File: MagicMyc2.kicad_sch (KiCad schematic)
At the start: 27 parts, among them J1 RGB, J2 SPI, J3 PowerSupply, J4 Aout, J5 GPIOs, J6 PRG, J7 MEM2080-00-128-00-A, J8 10102166A812A, Q1 BC338, U1 PIC18F15Q41-I/SS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

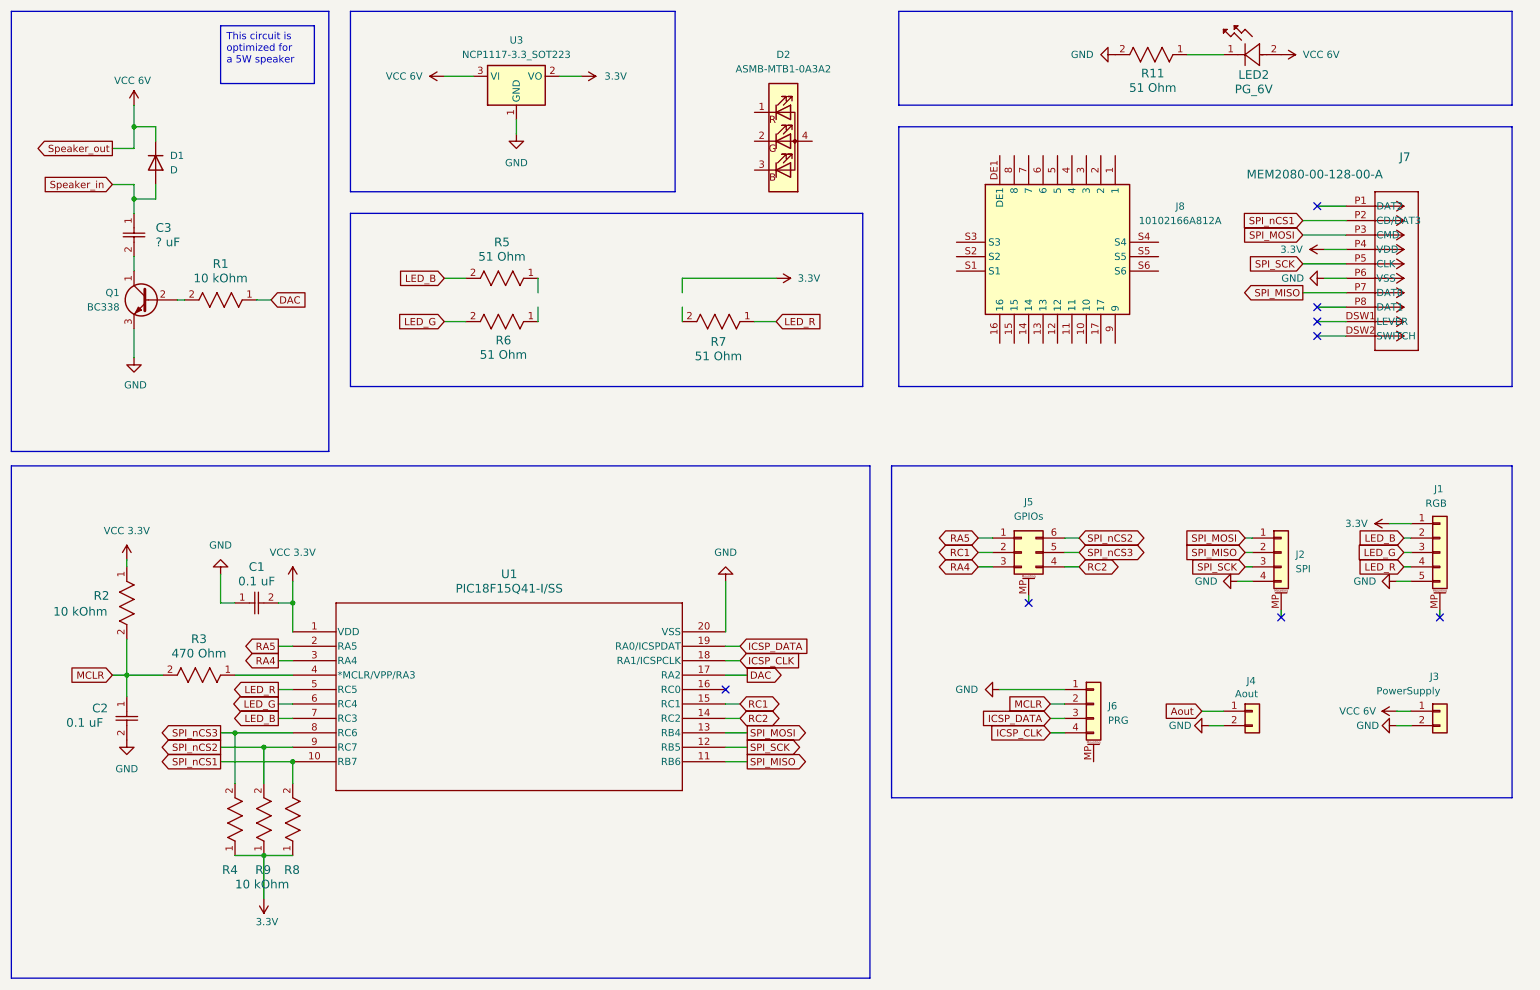
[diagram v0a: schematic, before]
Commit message: v2: changed Pinout, Layout; removed 6V PG-LED
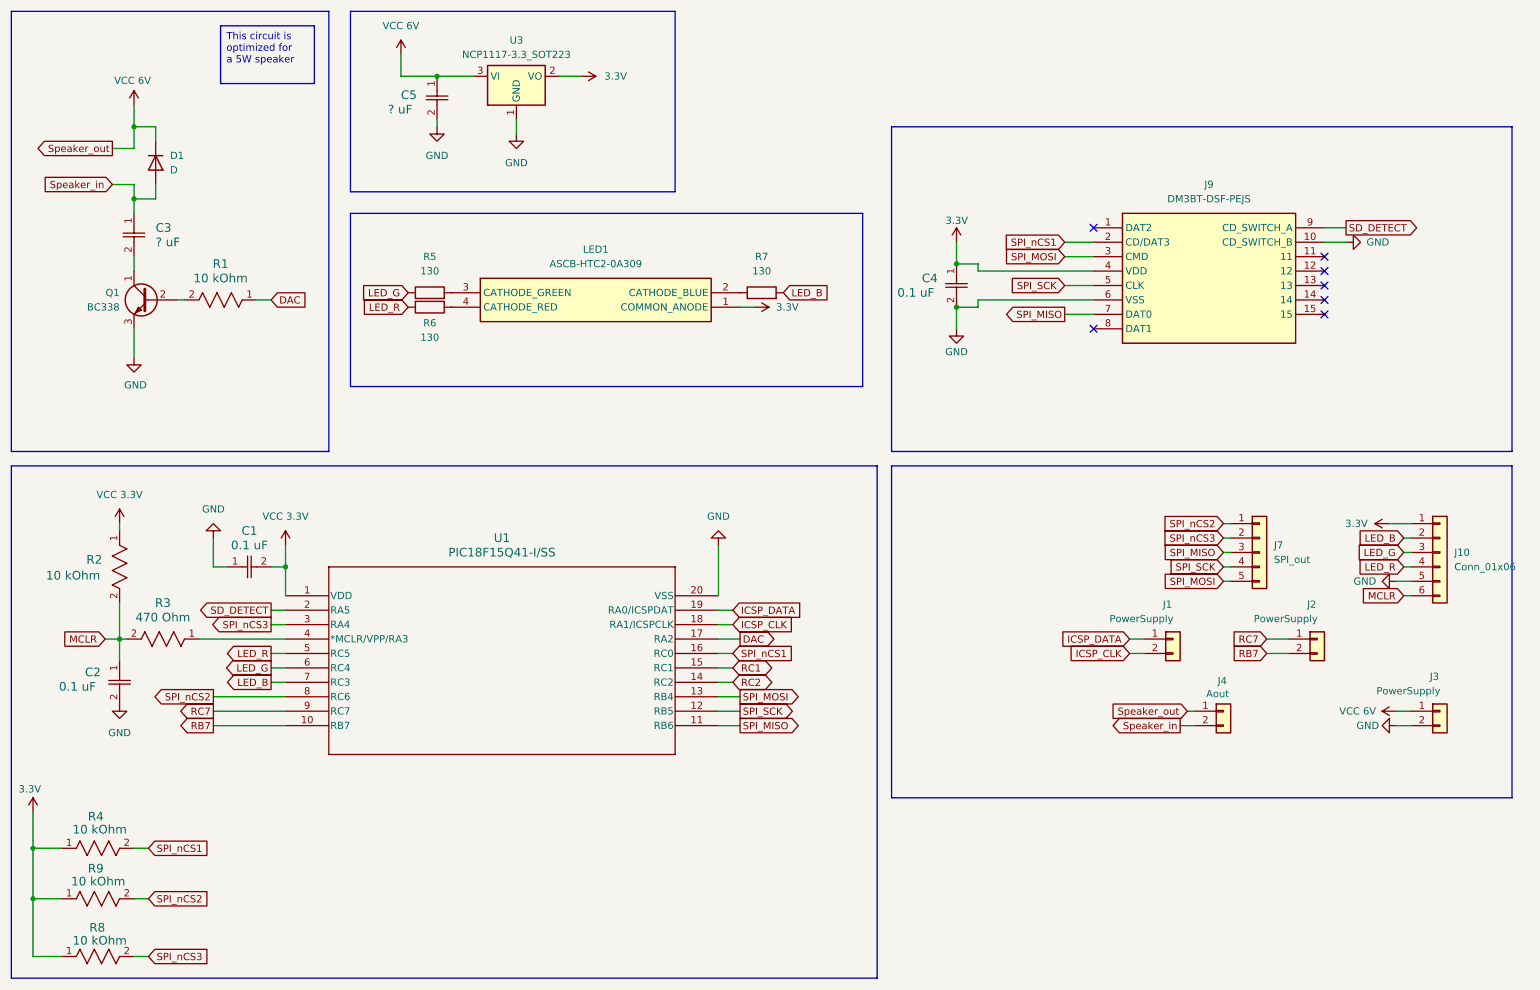
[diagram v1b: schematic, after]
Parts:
- removed D2: ASMB-MTB1-0A3A2, LED_SMD:LED_Wurth_150044M155260, symbol LED:ASMB-MTB1-0A3A2
- removed J1: RGB, Connector_Hirose:Hirose_DF13-05P-1.25DSA_1x05_P1.25mm_Vertical, symbol Connector_Generic_MountingPin:Conn_01x05_MountingPin
- removed J2: SPI, Connector_Hirose:Hirose_DF13-04P-1.25DSA_1x04_P1.25mm_Vertical, symbol Connector_Generic_MountingPin:Conn_01x04_MountingPin
- removed J5: GPIOs, Connector_PinHeader_2.00mm:PinHeader_2x03_P2.00mm_Vertical, symbol Connector_Generic_MountingPin:Conn_02x03_Counter_Clockwise_MountingPin
- removed J6: PRG, Connector_Hirose:Hirose_DF13-04P-1.25DSA_1x04_P1.25mm_Vertical, symbol Connector_Generic_MountingPin:Conn_01x04_MountingPin
- removed J7: MEM2080-00-128-00-A, MEM2080-00-128-00-A:CONN_MEM2080-00-128-00-A_GCT, symbol MEM2080-00-128-00-A:MEM2080-00-128-00-A
- removed J8: 10102166A812A, 10102166A812A, symbol 10102166A812A:10102166A812A
- removed LED2: PG_6V, JB3030AWT-P-B65EA0000-N0000001:LED_J-SERIES_3030_CRW, symbol JB3030AWT-P-B65EA0000-N0000001:JB3030AWT-P-B65EA0000-N0000001
- removed R11, R5, R6, R7: 51 Ohm, RT0603DRE0710KL:RC0603N_YAG, symbol RT0603DRE0751RL:RT0603DRE0751RL
- added C4: 0.1 uF, C0603C103M5RAC7411:CAPC17595_87N_KEM, symbol C0603C103M5RAC7411:C0603C103M5RAC7411
- added C5: ? uF, C0603C103M5RAC7411:CAPC17595_87N_KEM, symbol C0603C103M5RAC7411:C0603C103M5RAC7411
- added J1, J2: PowerSupply, Connector_PinHeader_2.00mm:PinHeader_1x02_P2.00mm_Vertical, symbol Connector_Generic:Conn_01x02
- added J10: Conn_01x06, Connector_PinHeader_2.00mm:PinHeader_1x06_P2.00mm_Vertical, symbol Connector_Generic:Conn_01x06
- added J7: SPI_out, Connector_PinHeader_2.00mm:PinHeader_1x05_P2.00mm_Vertical, symbol Connector_Generic:Conn_01x05
- added J9: DM3BT-DSF-PEJS, Connector_Card:microSD_HC_Hirose_DM3BT-DSF-PEJS, symbol DM3BT-DSF-PEJS:DM3BT-DSF-PEJS
- added LED1: ASCB-HTC2-0A309, ASCB-HTC2-0A309:ASCBHTC20A309, symbol ASCB-HTC2-0A309:ASCB-HTC2-0A309
- added R5, R6, R7: 130, Resistor_SMD:R_0603_1608Metric, symbol Device:R
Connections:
- net Aout is gone; now on net VCC 6V: J4.1 (Pin_1)
- net RA4 is gone; now on net SPI_nCS3: U1.3 (RA4)
- net 3.3V: now also C4.1, J10.1 (Pin_1), J9.4 (VDD), LED1.1 (COMMON_ANODE)
- net GND: now also C4.2, C5.2, J10.5 (Pin_5), J9.10 (CD_SWITCH_B), J9.6 (VSS); no longer J4.2 (Pin_2)
- net ICSP_CLK: now also J1.2 (Pin_2)
- net ICSP_DATA: now also J1.1 (Pin_1)
- net LED_B: now also J10.2 (Pin_2), R7.2
- net LED_G: now also J10.3 (Pin_3), R5.1
- net LED_R: now also J10.4 (Pin_4), R6.2
- net MCLR: now also J10.6 (Pin_6)
- net SPI_MISO: now also J7.3 (Pin_3), J9.7 (DAT0)
- net SPI_MOSI: now also J7.5 (Pin_5), J9.3 (CMD)
- net SPI_SCK: now also J7.4 (Pin_4), J9.5 (CLK)
- net SPI_nCS1: now also R4.2, U1.16 (RC0), J9.2 (CD/DAT3); no longer R8.2, U1.10 (RB7)
- net SPI_nCS2: now also U1.8 (RC6), J7.1 (Pin_1); no longer U1.9 (RC7)
- net SPI_nCS3: now also R8.2, J7.2 (Pin_2); no longer R4.2, U1.8 (RC6)
- net Speaker_in : now also J4.2 (Pin_2)
- net VCC 6V: now also C5.1
- net RA5 renamed SD_DETECT
- net SD_DETECT: now also J9.9 (CD_SWITCH_A)
- new net: LED1.3 (CATHODE_GREEN), R5.2
- new net: LED1.2 (CATHODE_BLUE), R7.1
- new net: LED1.4 (CATHODE_RED), R6.1
- new net RB7: J2.2 (Pin_2), U1.10 (RB7)
- new net RC7: J2.1 (Pin_1), U1.9 (RC7)
- no-connect marks 8 -> 7
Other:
- moved on the sheet: C1, C2, J4, R2, R3, R4, R8, R9, U1

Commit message: added drill holes back
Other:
- moved on the sheet: C4, C5, J9, LED1, R5, R6, R7, U3

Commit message: Updated schematic pdf + some 3D models
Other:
- company: (none) -> Author: Christian R
- title: (none) -> MagicMyc2
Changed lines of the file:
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@@
 	(generator_version "8.0")
 	(paper "A4")
+	(title_block
+		(title "MagicMyc2")
+		(date "26.01.2025")
+		(rev "2")
+		(company "Author: Christian R")
+	)
 	(junction
 		(at 39.37 49.53)

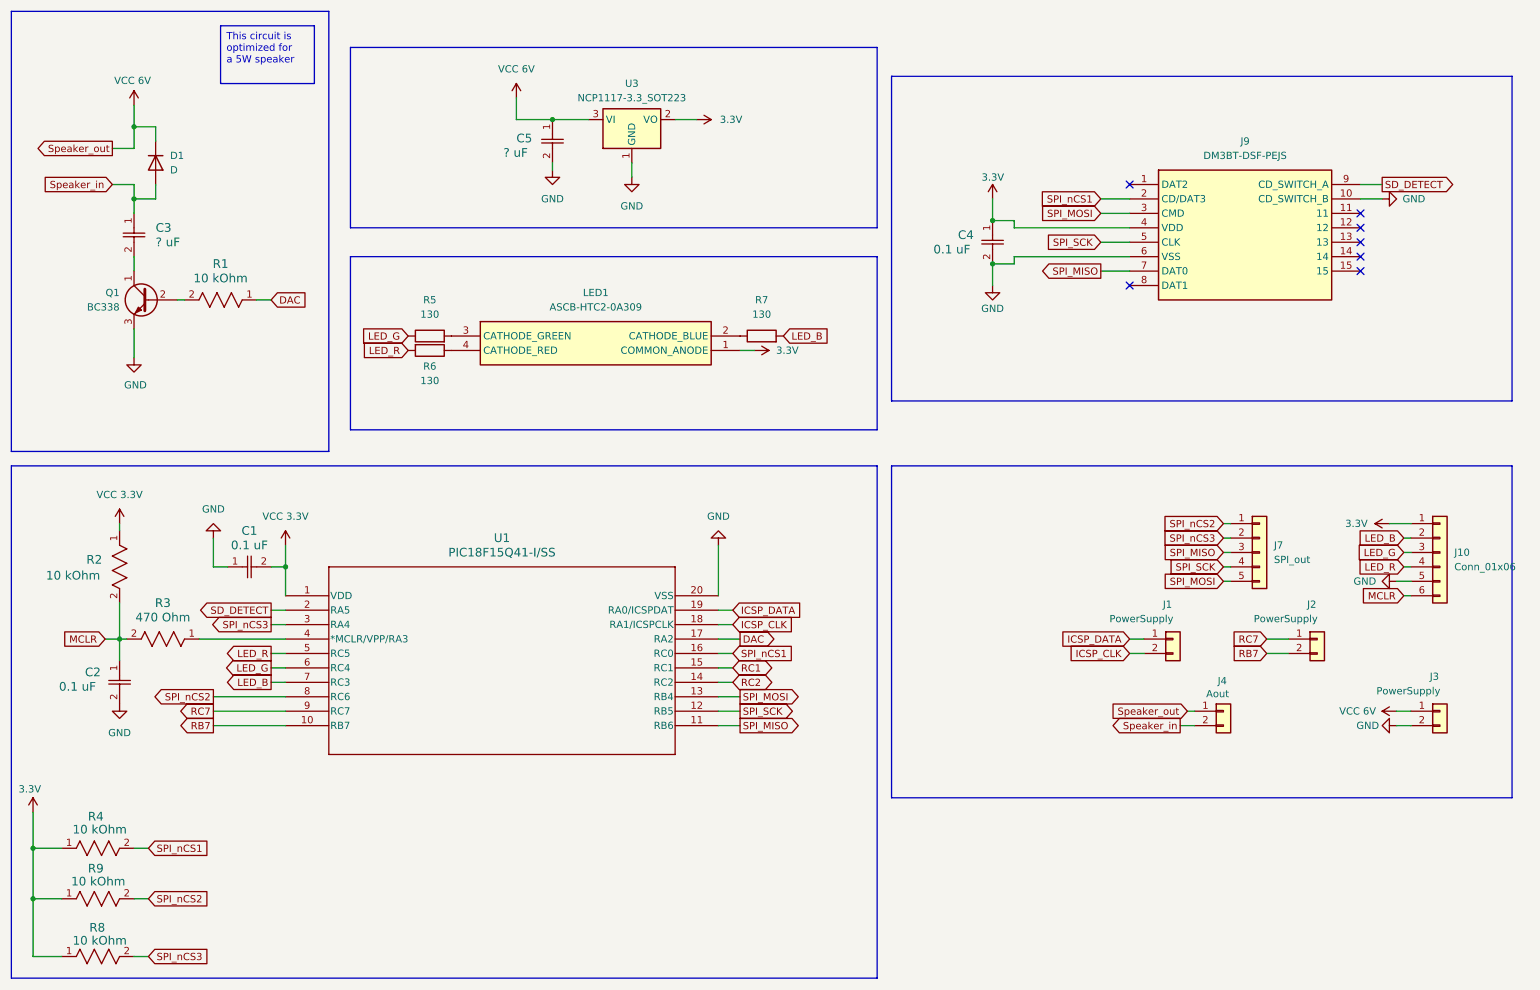
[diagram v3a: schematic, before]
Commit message: Added design optimizations + Removed little ground islands by increasing min area size + Added teardrops + Fixes (almost) all errors + Added another 130Ohm resistor for RGB-LED (green) to maximize green power
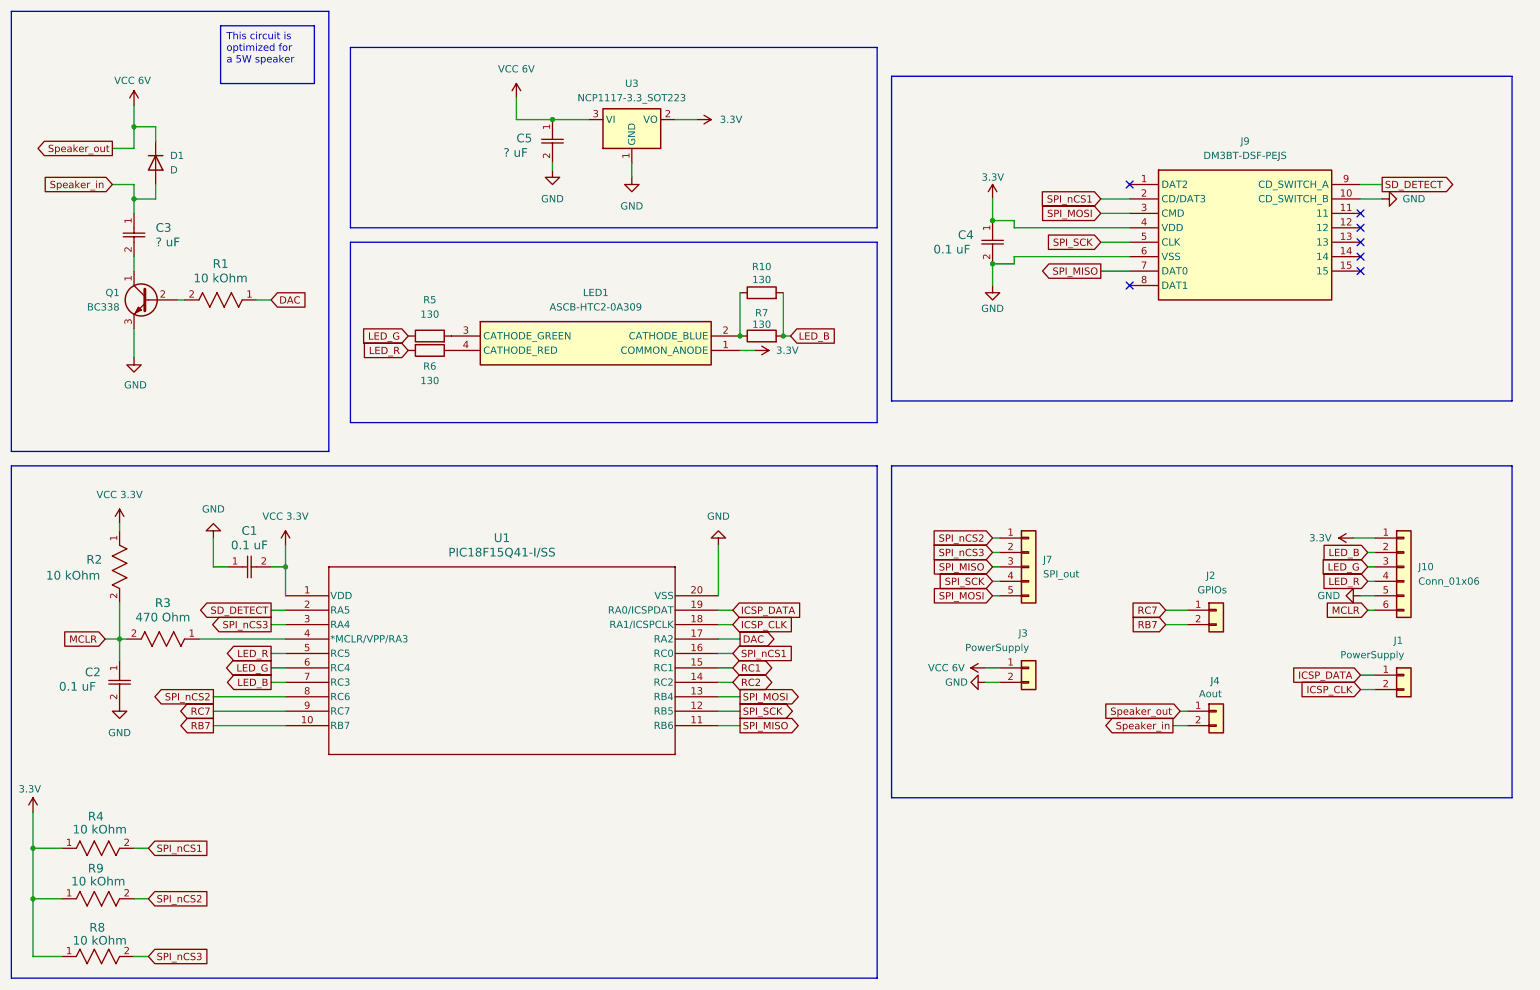
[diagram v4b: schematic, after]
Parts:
- added R10: 130, Resistor_SMD:R_0603_1608Metric, symbol Device:R
- J2: value PowerSupply -> GPIOs
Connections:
- net LED_B: now also R10.2
- net at LED1.2 (CATHODE_BLUE), R7.1: now also R10.1
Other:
- moved on the sheet: J1, J10, J2, J3, J4, J7

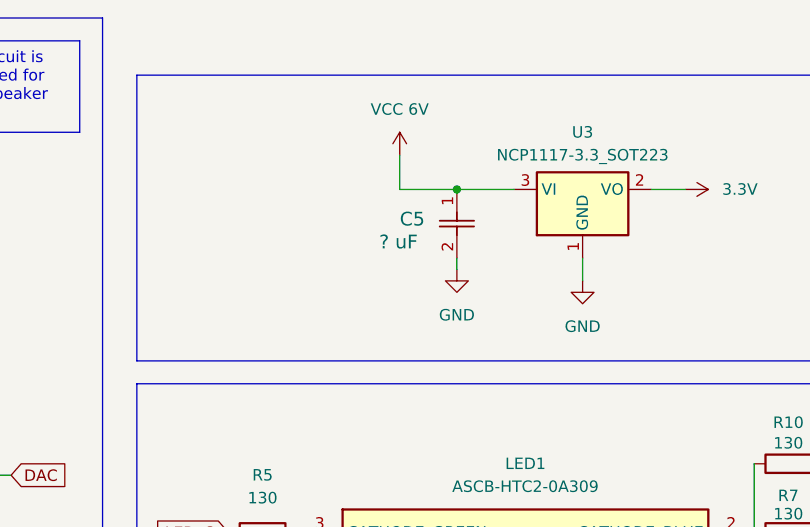
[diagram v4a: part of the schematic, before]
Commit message: Added rounded corners
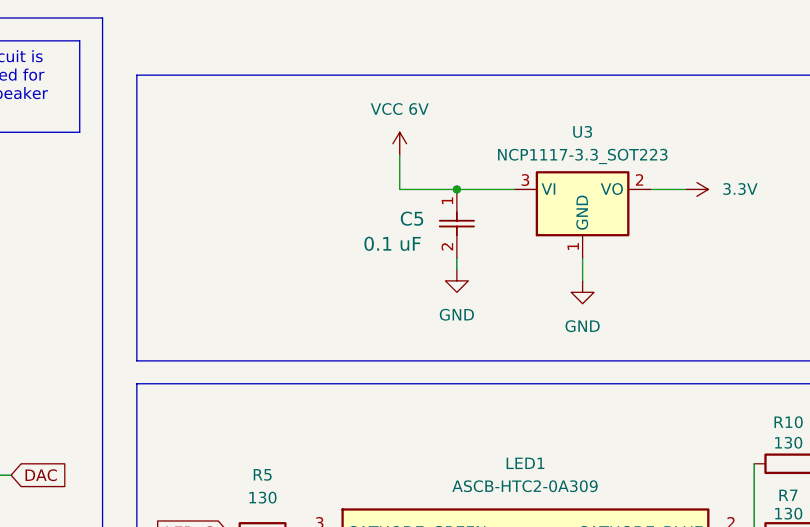
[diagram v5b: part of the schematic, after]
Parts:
- C5: value ? uF -> 0.1 uF
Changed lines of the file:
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@@
 			)
 		)
-		(property "Value" "? uF"
-			(at 104.394 41.402 90)
+		(property "Value" "0.1 uF"
+			(at 102.616 41.656 90)
 			(effects
 				(font
